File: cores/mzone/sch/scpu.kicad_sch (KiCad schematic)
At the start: 76 parts, among them X1 14.318MHZ

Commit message: mzone core
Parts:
- added unit 7 of A11
- added unit 2 of DE6
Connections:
- net GND: now also A11.7 (GND), DE6.14 (GND); no longer DE6.14 (GND)
- net VCC: now also A11.14 (VCC), DE6.1 (VPP), DE6.27 (~{PGM}), DE6.28 (VCC); no longer DE6.1 (VPP), DE6.26 (NC), DE6.27 (~{PGM}), DE6.28 (VCC)
- no-connect marks 54 -> 55
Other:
- note added: "KOLLA MUTE!"
- moved on the sheet: B_B6E, B_C3B, C4, C9

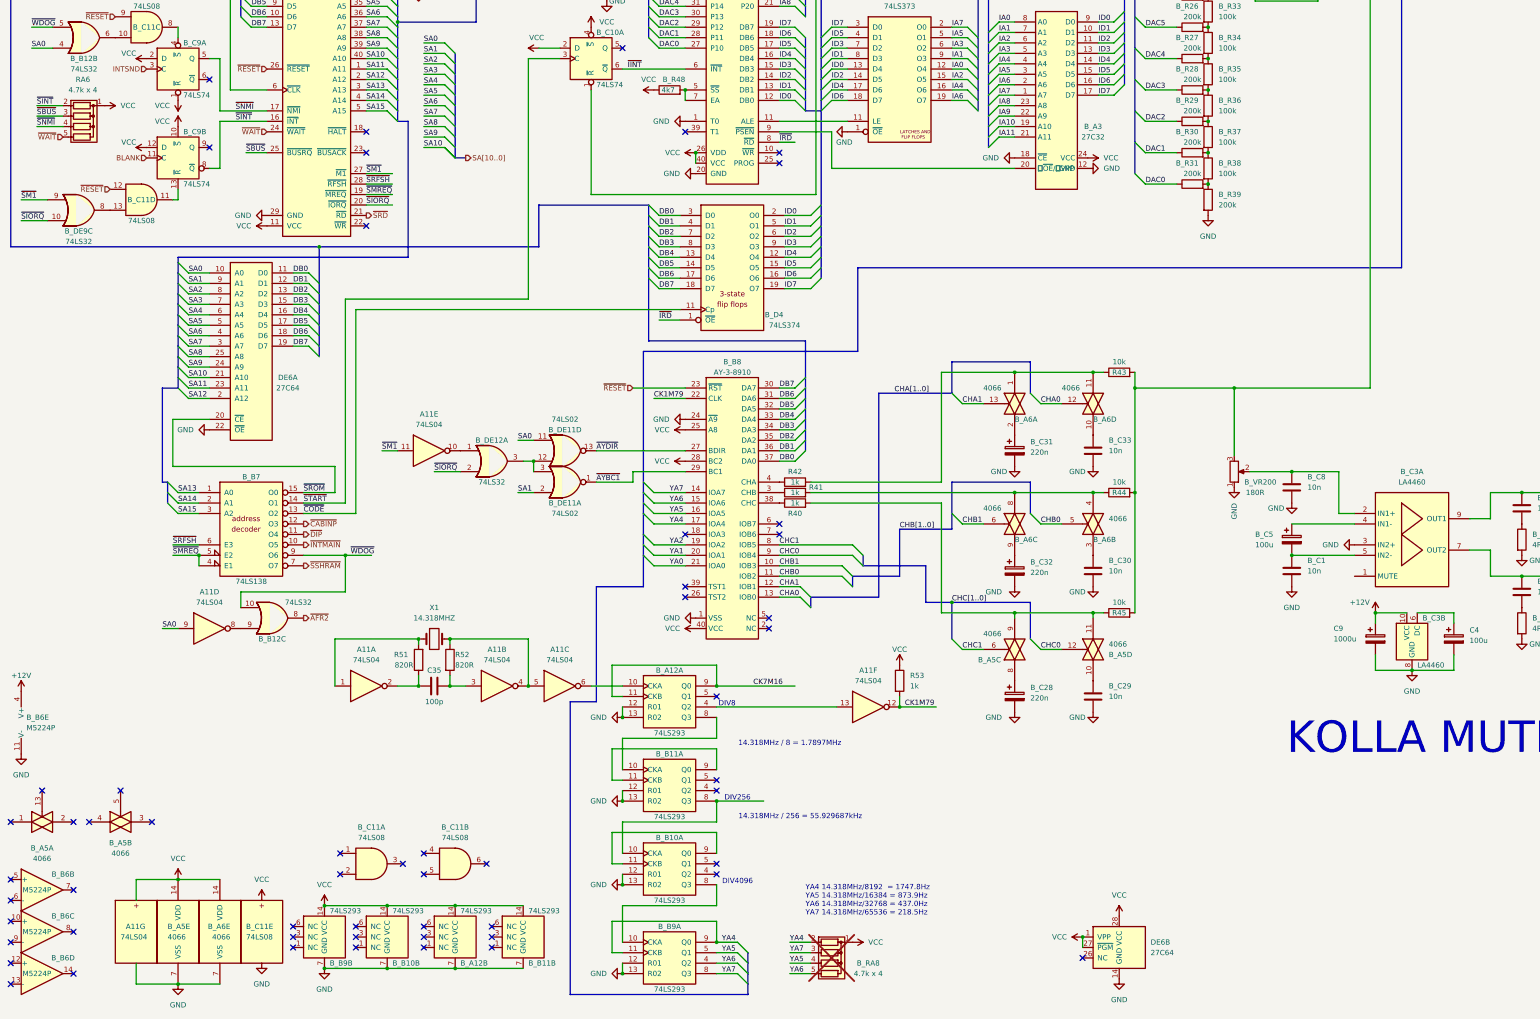
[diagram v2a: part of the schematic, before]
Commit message: mzone core
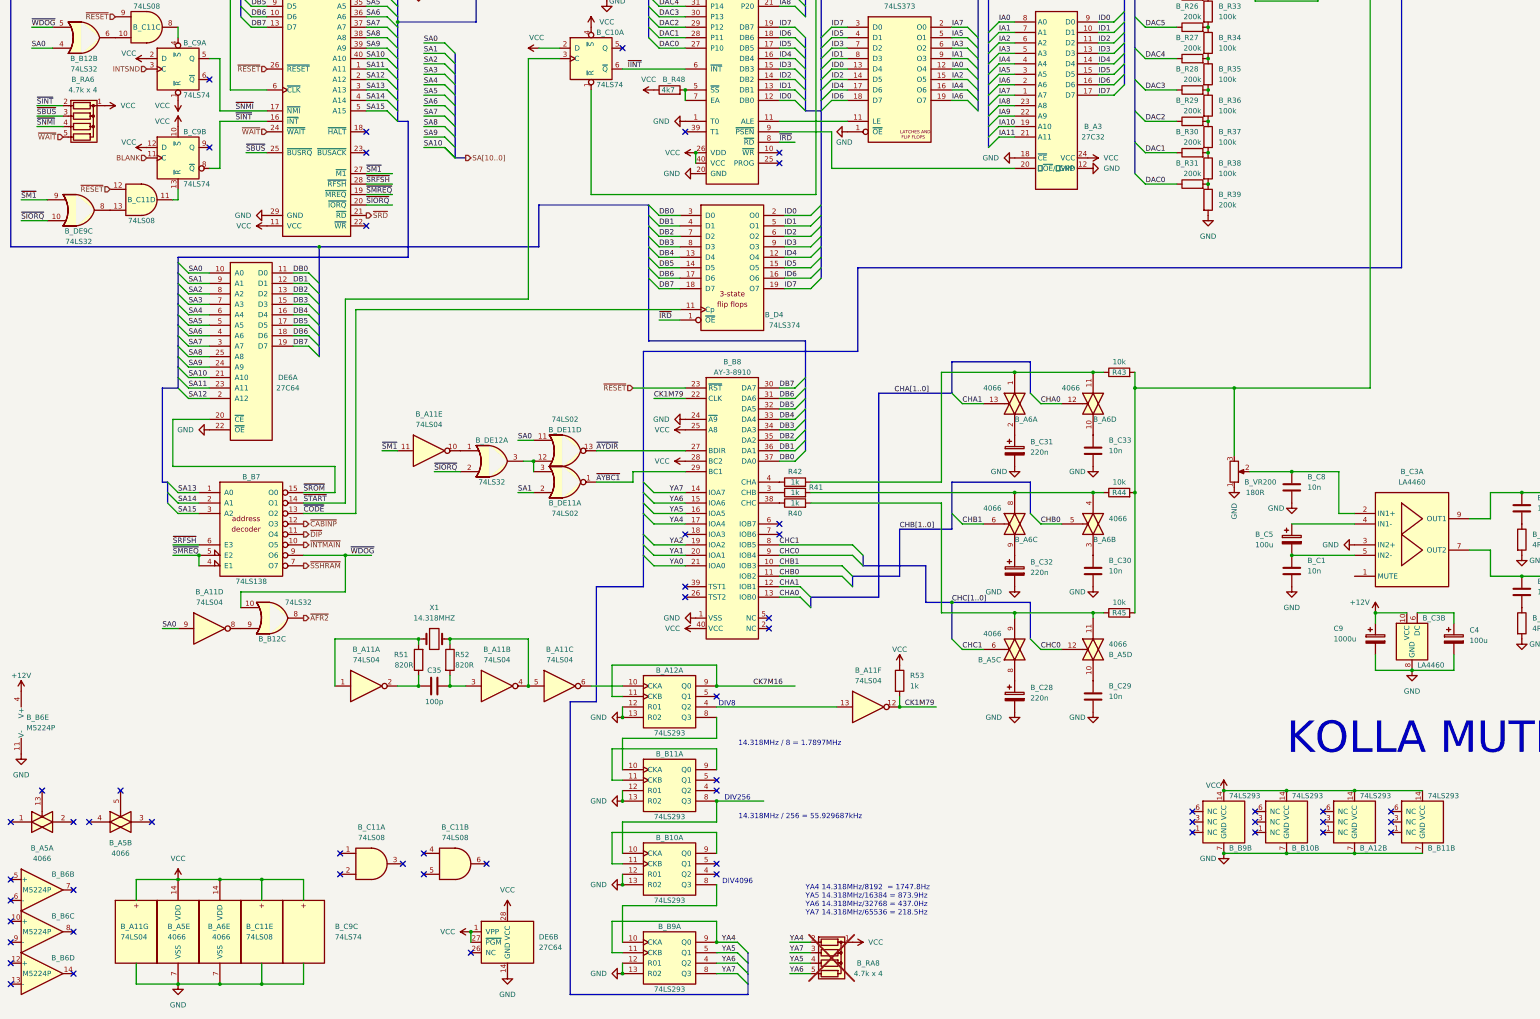
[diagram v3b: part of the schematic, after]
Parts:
- added unit 3 of B_C9
- renumbered A11 to B_A11, RA6 to B_RA6
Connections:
- net GND: now also B_C9.7 (GND)
- net VCC: now also B_C9.14 (VCC)
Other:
- moved on the sheet: B_A12B, B_B10B, B_B11B, B_B9B, DE6B

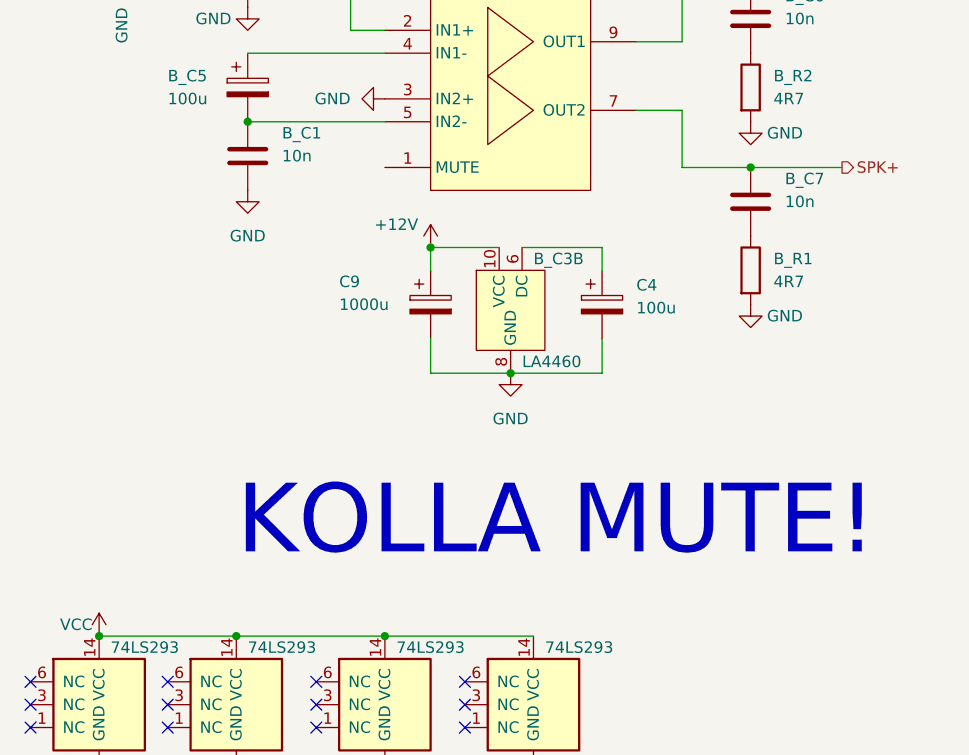
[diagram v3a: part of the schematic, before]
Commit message: mzone core
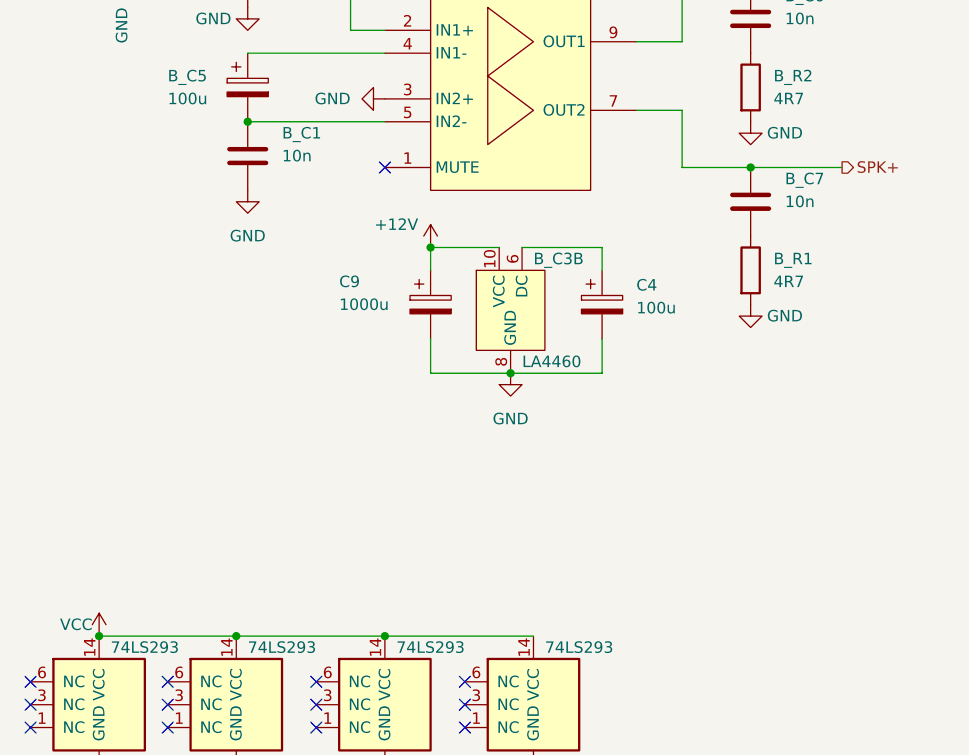
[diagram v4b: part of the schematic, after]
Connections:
- no-connect marks 55 -> 56
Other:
- note removed: "KOLLA MUTE!"

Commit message: mzone core
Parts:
- added unit 2 of B_A2
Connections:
- net GND: now also B_A2.10 (GND); no longer B_A2.10 (GND)
- net VCC: now also B_A2.20 (VCC); no longer B_A2.20 (VCC)

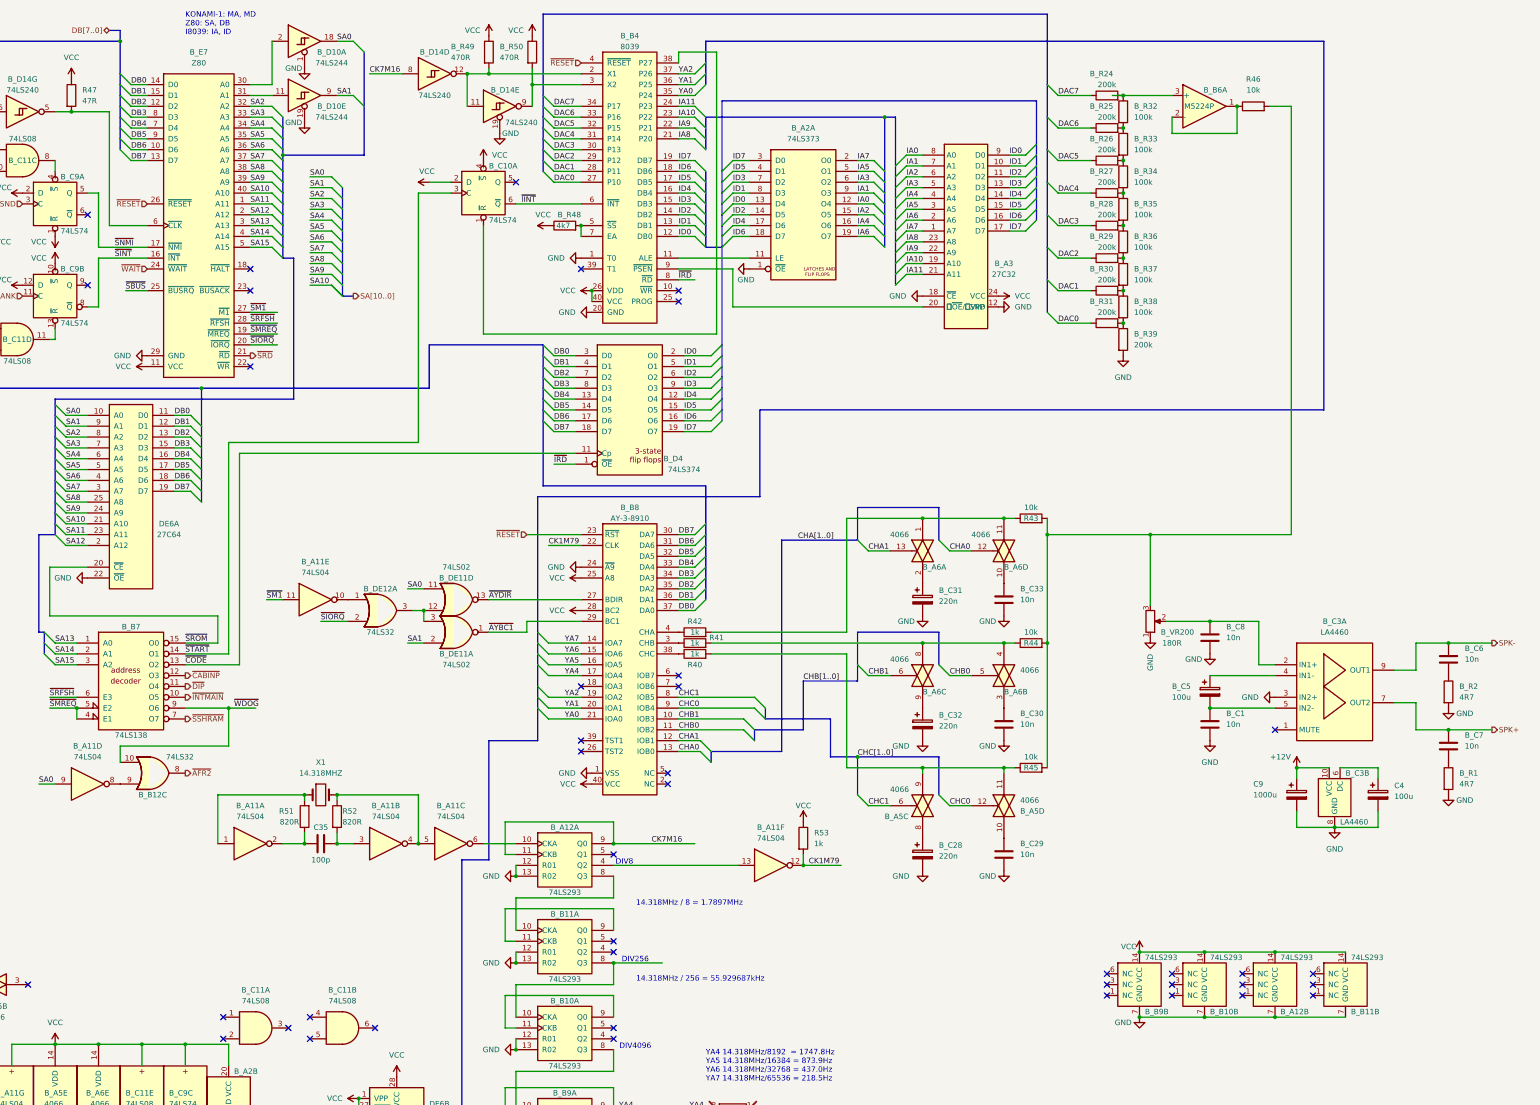
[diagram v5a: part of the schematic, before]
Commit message: mzone core
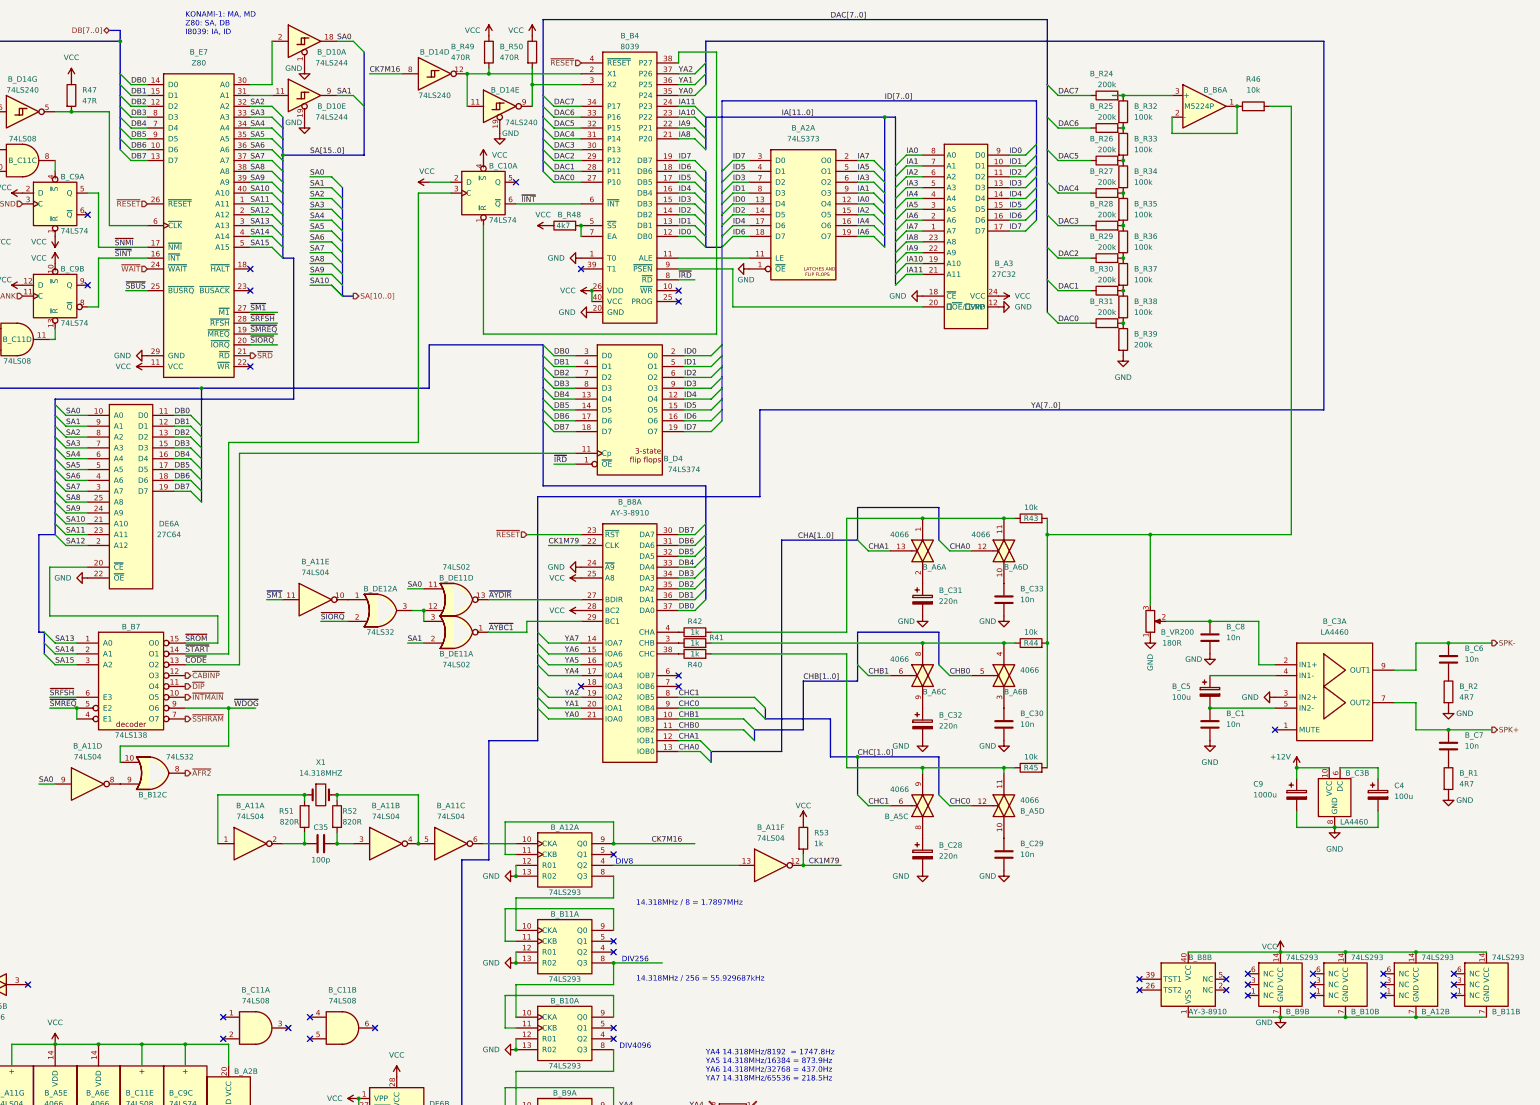
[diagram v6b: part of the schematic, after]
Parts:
- removed B_B8: AY-3-8910, symbol skutis:AY-3-8910
- added B_B8: AY-3-8910, symbol arcade:AY-3-8910
- B_C3: symbol skutis:LA4460 -> arcade:LA4460
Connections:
- net CHA0: now also B_B8.13 (IOB0)
- net CHA1: now also B_B8.12 (IOB1)
- net CHB0: now also B_B8.11 (IOB2)
- net CHB1: now also B_B8.10 (IOB3)
- net CHC0: now also B_B8.9 (IOB4)
- net CHC1: now also B_B8.8 (IOB5)
- net CK1M79: now also B_B8.22 (CLK)
- net DB0: now also B_B8.37 (DA0)
- net DB1: now also B_B8.36 (DA1)
- net DB2: now also B_B8.35 (DA2)
- net DB3: now also B_B8.34 (DA3)
- net DB4: now also B_B8.33 (DA4)
- net DB5: now also B_B8.32 (DA5)
- net DB6: now also B_B8.31 (DA6)
- net DB7: now also B_B8.30 (DA7)
- net GND: now also B_B7.8 (GND), B_B8.1 (VSS), B_B8.24 (~{A9})
- net VCC: now also B_B7.16 (VCC), B_B8.25 (A8), B_B8.28 (BC2), B_B8.40 (VCC)
- net YA0: now also B_B8.21 (IOA0)
- net YA1: now also B_B8.20 (IOA1)
- net YA2: now also B_B8.19 (IOA2)
- net YA4: now also B_B8.17 (IOA4)
- net YA5: now also B_B8.16 (IOA5)
- net YA6: now also B_B8.15 (IOA6)
- net YA7: now also B_B8.14 (IOA7)
- net ~{AYBC1}: now also B_B8.29 (BC1)
- net ~{AYDIR}: now also B_B8.27 (BDIR)
- net ~{RESET}: now also B_B8.23 (~{RST})
- net at R40.1: now also B_B8.38 (CHC)
- net at R41.1: now also B_B8.3 (CHB)
- net at R42.1: now also B_B8.4 (CHA)
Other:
- company: (none) -> Konami GX319
- title: (none) -> Megazone
- moved on the sheet: B_A12B, B_B10B, B_B11B, B_B9B
